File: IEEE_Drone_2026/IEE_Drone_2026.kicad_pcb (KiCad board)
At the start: 2 copper layers, 40.5 x 58 mm, 30 parts, among them IC1 TPSM84209RKHT, IC2 TPSM84209RKHT, J1 ESC, J10 M2, J11 Conn_01x02_Socket, J2 M4 Mounting, J3 M4 Mounting, J4 M4 Mounting, J5 M4 Mounting, J6 Pixy2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

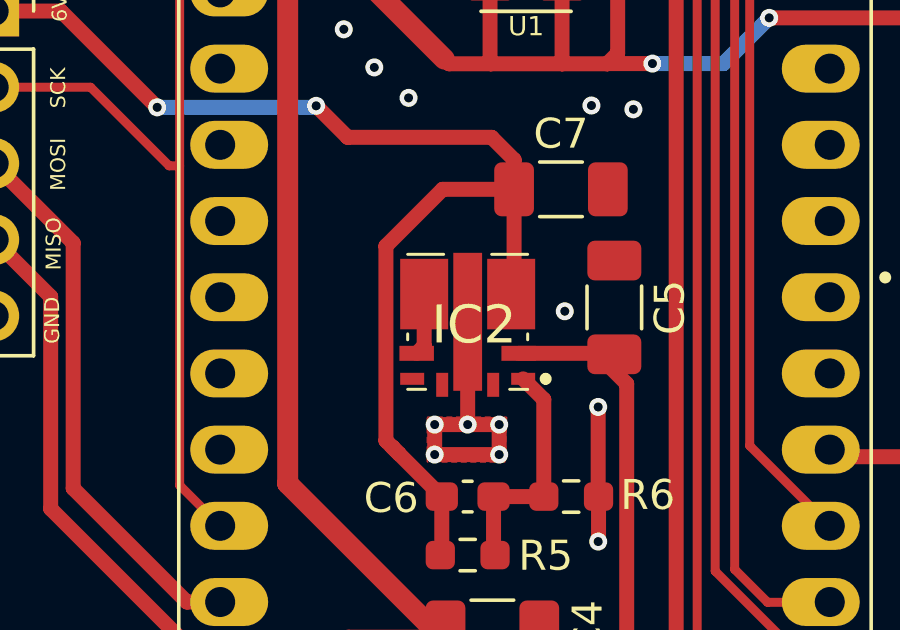
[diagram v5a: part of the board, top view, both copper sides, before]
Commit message: fixed DRC problems, 0 errors
keepout errors from the fill to remove gnd
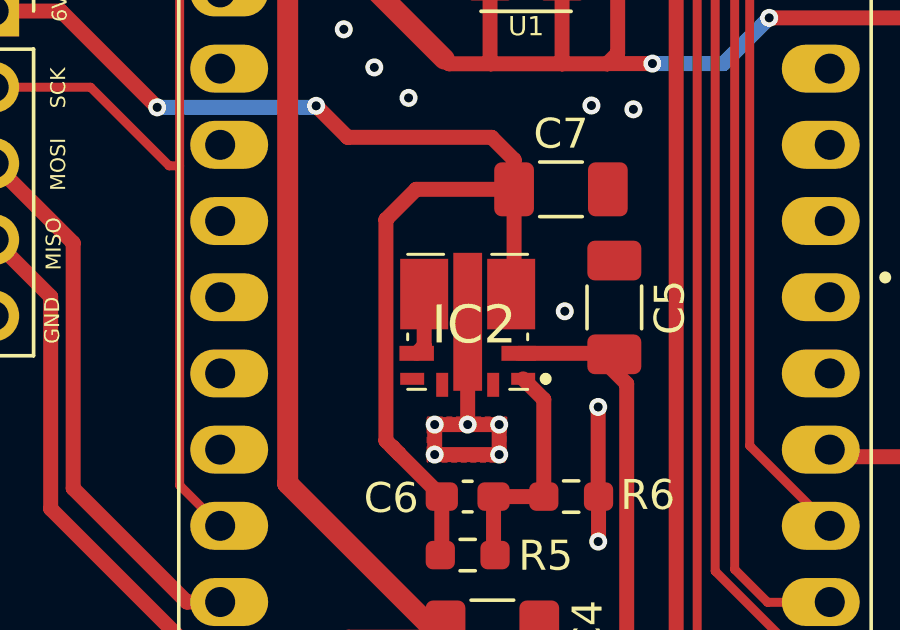
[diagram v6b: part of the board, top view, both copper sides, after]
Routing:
- net 6V: track 40.4 -> 40.9 mm
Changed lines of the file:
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@@
+	)
+	(segment
+		(start 69.69 61.24)
+		(end 67.45 61.24)
+		(width 0.5)
+		(layer "F.Cu")
+		(net 34)
+	)
+	(segment
+		(start 84.05 65.45)
+		(end 79.25 65.45)
+		(width 0.5)
+		(layer "F.Cu")
+		(net 34)
+	)
+	(segment
+		(start 84.05 65.45)
+		(end 84.7975 66.1975)
+		(width 0.5)
+		(layer "F.Cu")
+		(net 34)
+	)
+	(segment
+		(start 72.9 64.45)
+		(end 69.69 61.24)
+		(width 0.5)
+		(layer "F.Cu")
+		(net 34)
+	)
+	(segment
+		(start 84.7975 70.5775)
+		(end 84.7 70.675)
+		(width 0.5)
+		(layer "F.Cu")
+		(net 34)
+	)
+	(segment
+		(start 82.3875 77.425)
+		(end 80.96875 76.00625)
+		(width 0.5)
+		(layer "F.Cu")
+		(net 34)
+	)
+	(segment
+		(start 82.3875 77.425)
+		(end 82.3875 79.325)
+		(width 0.5)
+		(layer "F.Cu")
+		(net 34)
+	)
+	(segment
+		(start 80.524 68.193)
+		(end 81.534 67.183)
+		(width 0.5)
+		(layer "F.Cu")
+		(net 34)
+	)
+	(segment
+		(start 79.25 65.45)
+		(end 78.2 64.4)
+		(width 0.5)
+		(layer "F.Cu")
+		(net 34)
+	)
+	(segment
+		(start 81.534 67.183)
+		(end 84.7975 67.183)
+		(width 0.5)
+		(layer "F.Cu")
+		(net 34)
 	)
 	(segment
@@
 	)
 	(segment
-		(start 69.69 61.24)
-		(end 67.45 61.24)
-		(width 0.5)
-		(layer "F.Cu")
-		(net 34)
-	)
-	(segment
-		(start 84.05 65.45)
-		(end 79.25 65.45)
-		(width 0.5)
-		(layer "F.Cu")
-		(net 34)
-	)
-	(segment
-		(start 84.05 65.45)
-		(end 84.7975 66.1975)
-		(width 0.5)
-		(layer "F.Cu")
-		(net 34)
-	)
-	(segment
-		(start 72.9 64.45)
-		(end 69.69 61.24)
-		(width 0.5)
-		(layer "F.Cu")
-		(net 34)
-	)
-	(segment
-		(start 84.7975 70.5775)
-		(end 84.7 70.675)
-		(width 0.5)
-		(layer "F.Cu")
-		(net 34)
-	)
-	(segment
-		(start 82.3875 77.425)
-		(end 80.96875 76.00625)
-		(width 0.5)
-		(layer "F.Cu")
-		(net 34)
-	)
-	(segment
-		(start 82.3875 77.425)
-		(end 82.3875 79.325)
-		(width 0.5)
-		(layer "F.Cu")
-		(net 34)
-	)
-	(segment
-		(start 79.25 65.45)
-		(end 78.2 64.4)
-		(width 0.5)
-		(layer "F.Cu")
-		(net 34)
-	)
-	(segment
-		(start 80.524 75.5615)
-		(end 80.524 69.074)
-		(width 0.5)
-		(layer "F.Cu")
-		(net 34)
-	)
-	(segment
-		(start 82.415 67.183)
-		(end 84.7975 67.183)
-		(width 0.5)
-		(layer "F.Cu")
-		(net 34)
-	)
-	(segment
 		(start 80.96875 76.00625)
 		(end 80.75 75.7875)
@@
 	)
 	(segment
-		(start 80.524 69.074)
-		(end 82.415 67.183)
+		(start 80.524 75.5615)
+		(end 80.524 68.193)
 		(width 0.5)
 		(layer "F.Cu")
@@
 		(polygon
 			(pts
-				(xy 81.661 67.691) (xy 84.328 67.818) (xy 84.201 69.342) (xy 82.677 69.469) (xy 81.534 69.342)
+				(xy 81.661 67.691) (xy 83.693 68.072) (xy 84.074 69.088) (xy 82.677 69.088) (xy 81.534 68.961)
 			)
 		)

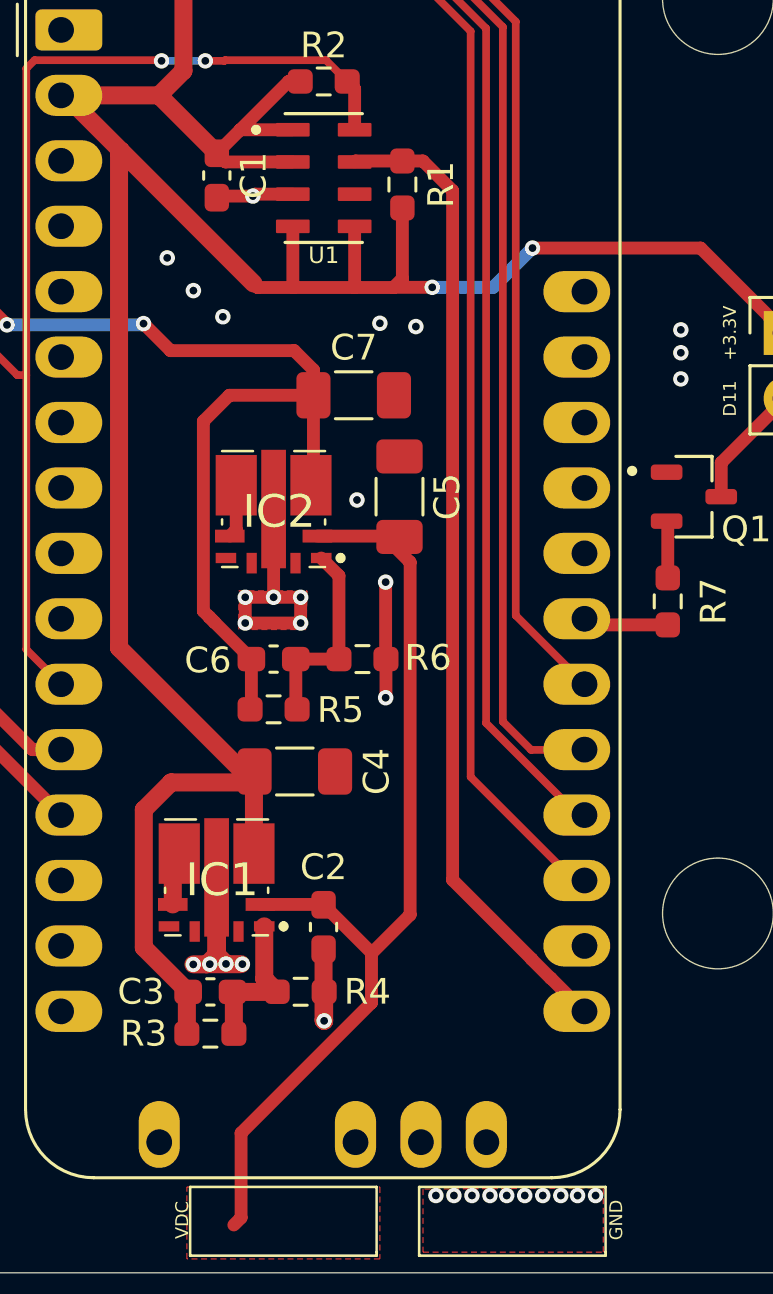
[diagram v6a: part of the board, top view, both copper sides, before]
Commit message: added a switch for VDC
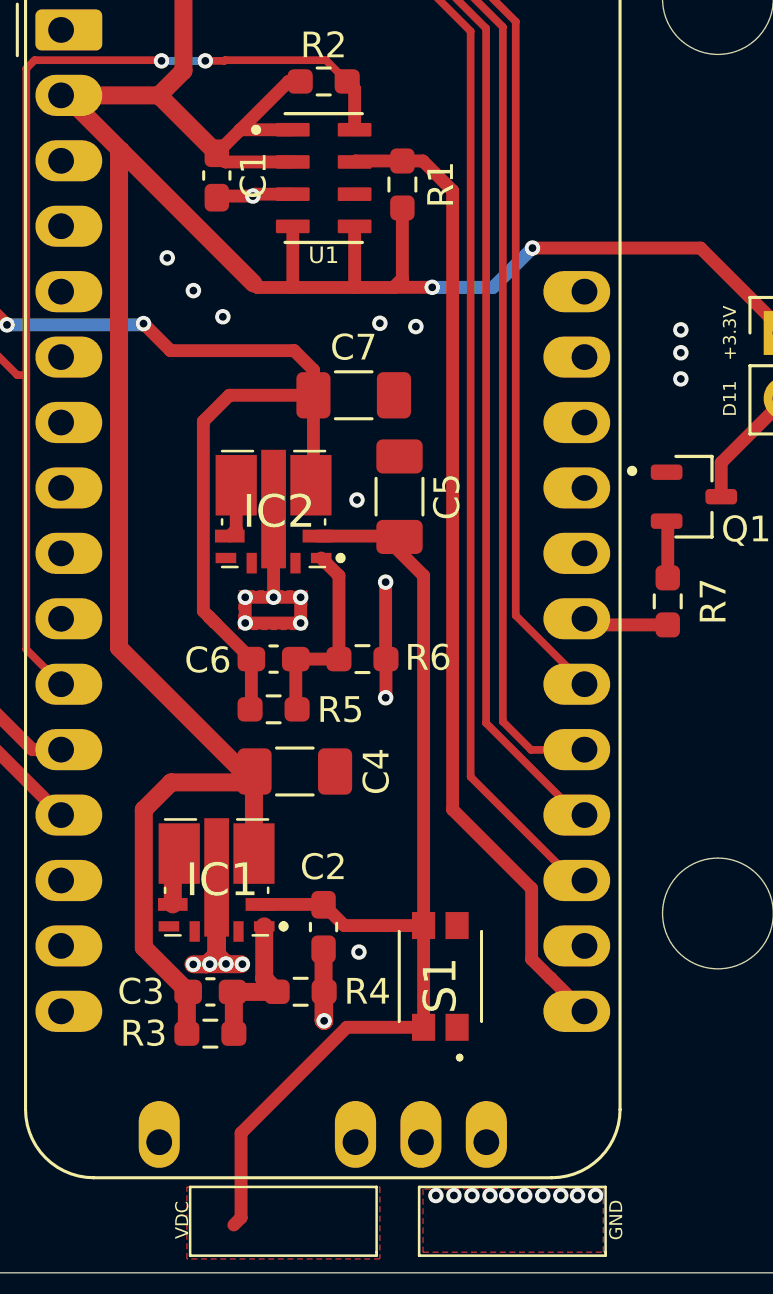
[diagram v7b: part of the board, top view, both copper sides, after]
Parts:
- added S1: SKTHAHE010, 16vbig:SKTHAHE010, F.Cu at (89.7, 89.7)
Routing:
- net +VDC: track 37.7 -> 41.4 mm
- net GND: vias 32 -> 33
